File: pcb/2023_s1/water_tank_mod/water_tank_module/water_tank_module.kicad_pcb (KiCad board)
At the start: 2 copper layers, 9 parts

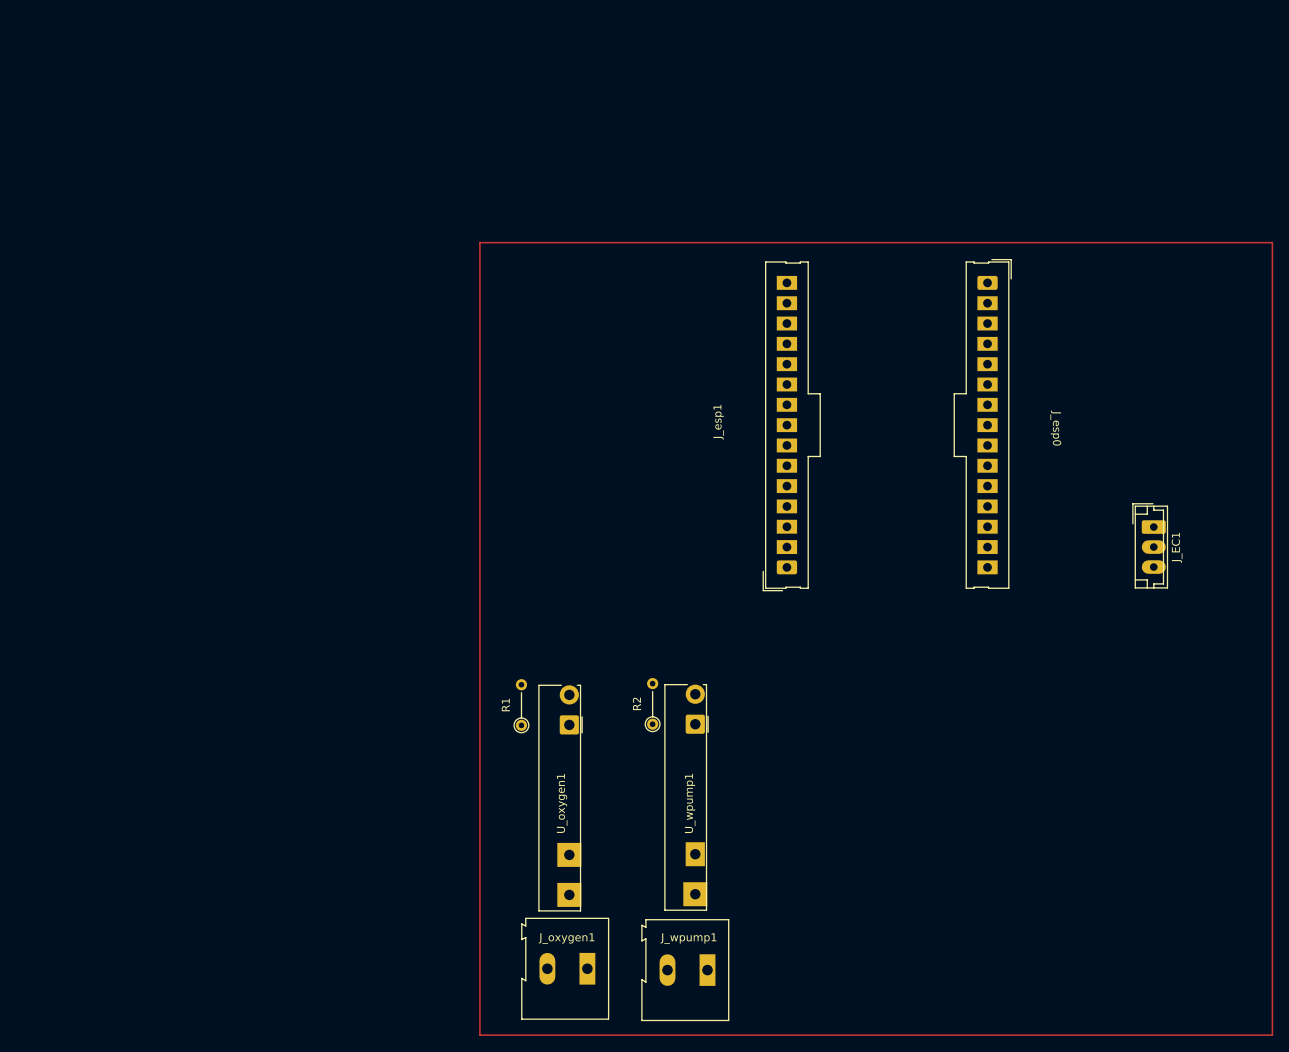
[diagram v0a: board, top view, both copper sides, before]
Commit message: water tank update, adn separation into control and power module
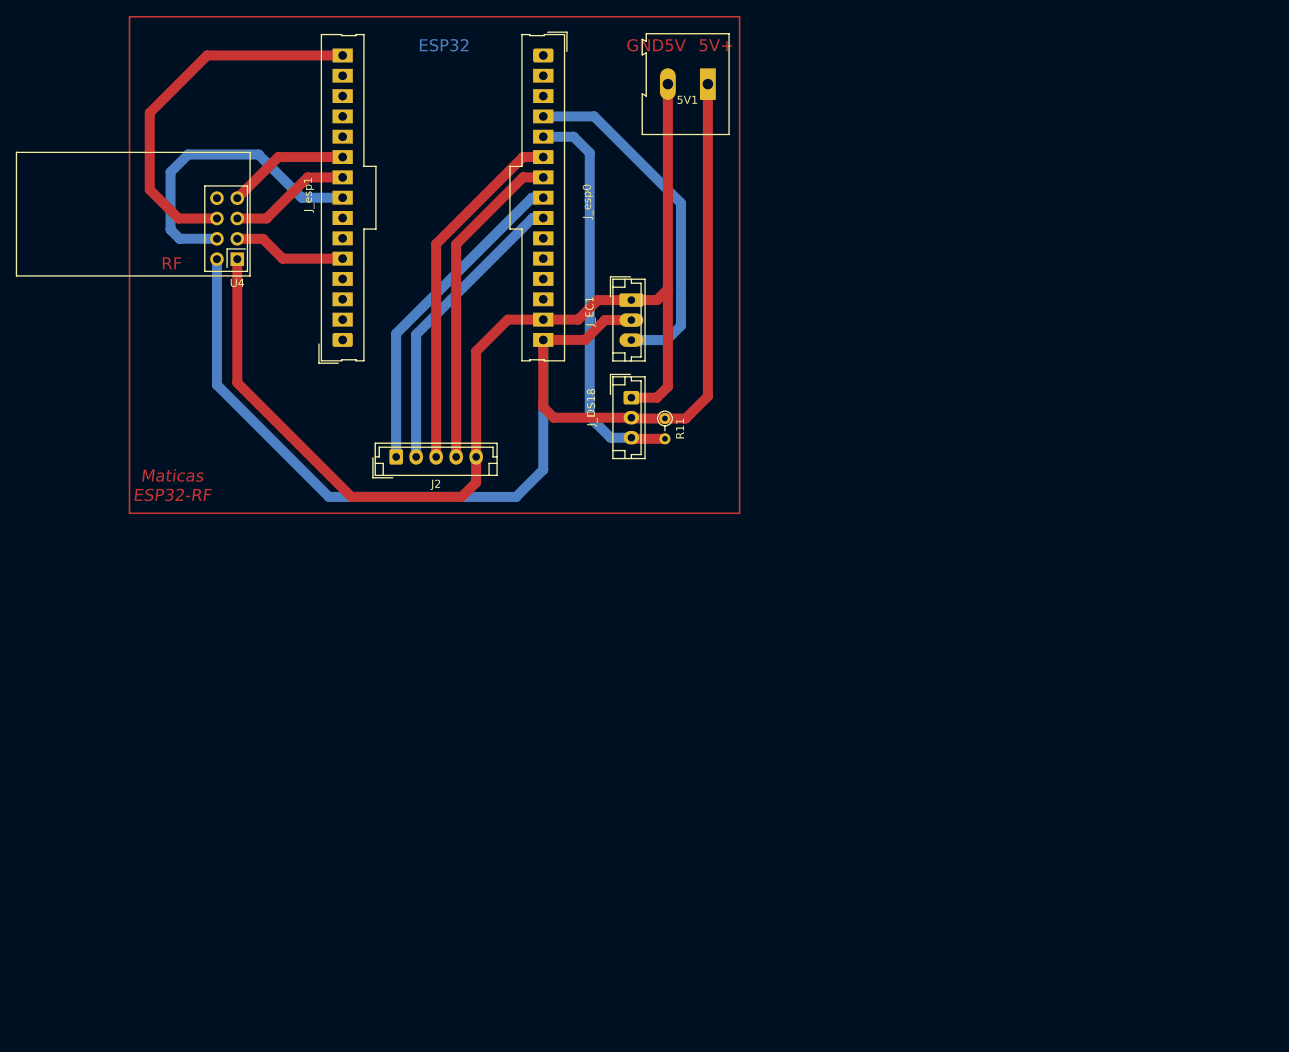
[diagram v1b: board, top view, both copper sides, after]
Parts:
- removed J_oxygen1, J_wpump1: Screw_Terminal_01x02, TerminalBlock:TerminalBlock_Altech_AK300-2_P5.00mm
- removed R1, R2: R, Resistor_THT:R_Axial_DIN0204_L3.6mm_D1.6mm_P5.08mm_Vertical
- removed U_oxygen1, U_wpump1: 34.81-8240, OptoDevice:Finder_34.81
- added 5V1: Screw_Terminal_01x02, TerminalBlock:TerminalBlock_Altech_AK300-2_P5.00mm, F.Cu at (130.1, 31.0)
- added J2: Conn_01x05_Male, Connector_JST:JST_EH_B5B-EH-A_1x05_P2.50mm_Vertical, F.Cu at (91.1, 77.6)
- added J_DS18: Conn_01x03_Male, Connector_JST:JST_EH_B3B-EH-A_1x03_P2.50mm_Vertical, F.Cu at (120.5, 70.2)
- added R11: 4.7k, Resistor_THT:R_Axial_DIN0204_L3.6mm_D1.6mm_P2.54mm_Vertical, F.Cu at (124.7, 72.8)
- added U4: NRF24L01_Breakout, RF_Module:nRF24L01_Breakout, F.Cu at (71.3, 52.9)
- moved J_EC1 71.2 mm to (120.5, 58.0)
- moved J_esp0 62.4 mm to (117.7, 45.6)
- moved J_esp1 62.4 mm to (76.3, 44.7)
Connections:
- J_EC1 pad 1: D34 -> GND5V
- J_EC1 pad 2: GND -> 5v
- J_EC1 pad 3: VIN -> D34
- J_esp0 pad 14: GND -> GND5V
- J_esp0 pad 15: VIN -> 5v
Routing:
- net 5v: track 0.00 -> 161.8 mm
- net GND5V: track 0.00 -> 138.6 mm
- net D35: track 0.00 -> 50.2 mm
- net D23: track 0.00 -> 46.6 mm
- net D32: track 0.00 -> 44.5 mm
- net D34: track 0.00 -> 44.0 mm
- net D33: track 0.00 -> 40.9 mm
- net D25: track 0.00 -> 40.8 mm
- net D5: track 0.00 -> 38.1 mm
- net D26: track 0.00 -> 37.2 mm
- net D19: track 0.00 -> 15.3 mm
- net D18: track 0.00 -> 15.3 mm
- net D4: track 0.00 -> 14.2 mm
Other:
- board text added: "5V+"
- board text added: "ESP32"
- board text added: "GND5V"
- board text added: "Maticas ESP32-RF"
- board text added: "RF"
